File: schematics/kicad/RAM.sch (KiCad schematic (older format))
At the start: 4 parts

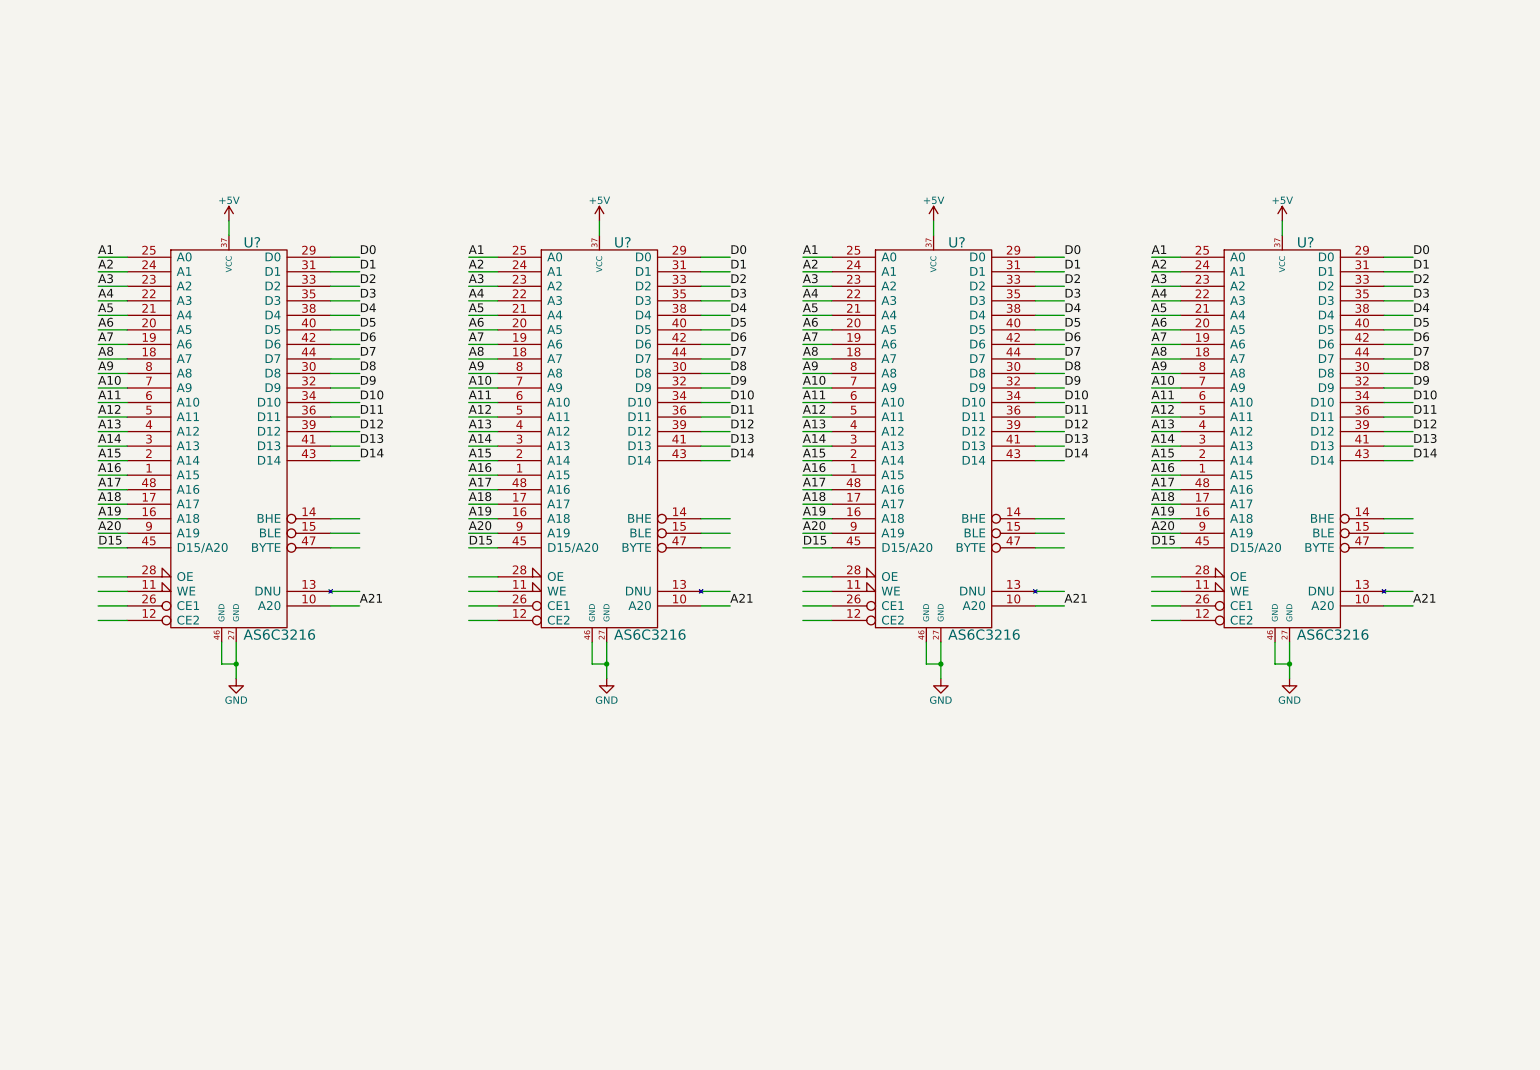
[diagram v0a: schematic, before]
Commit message: Add many hierarchical pins
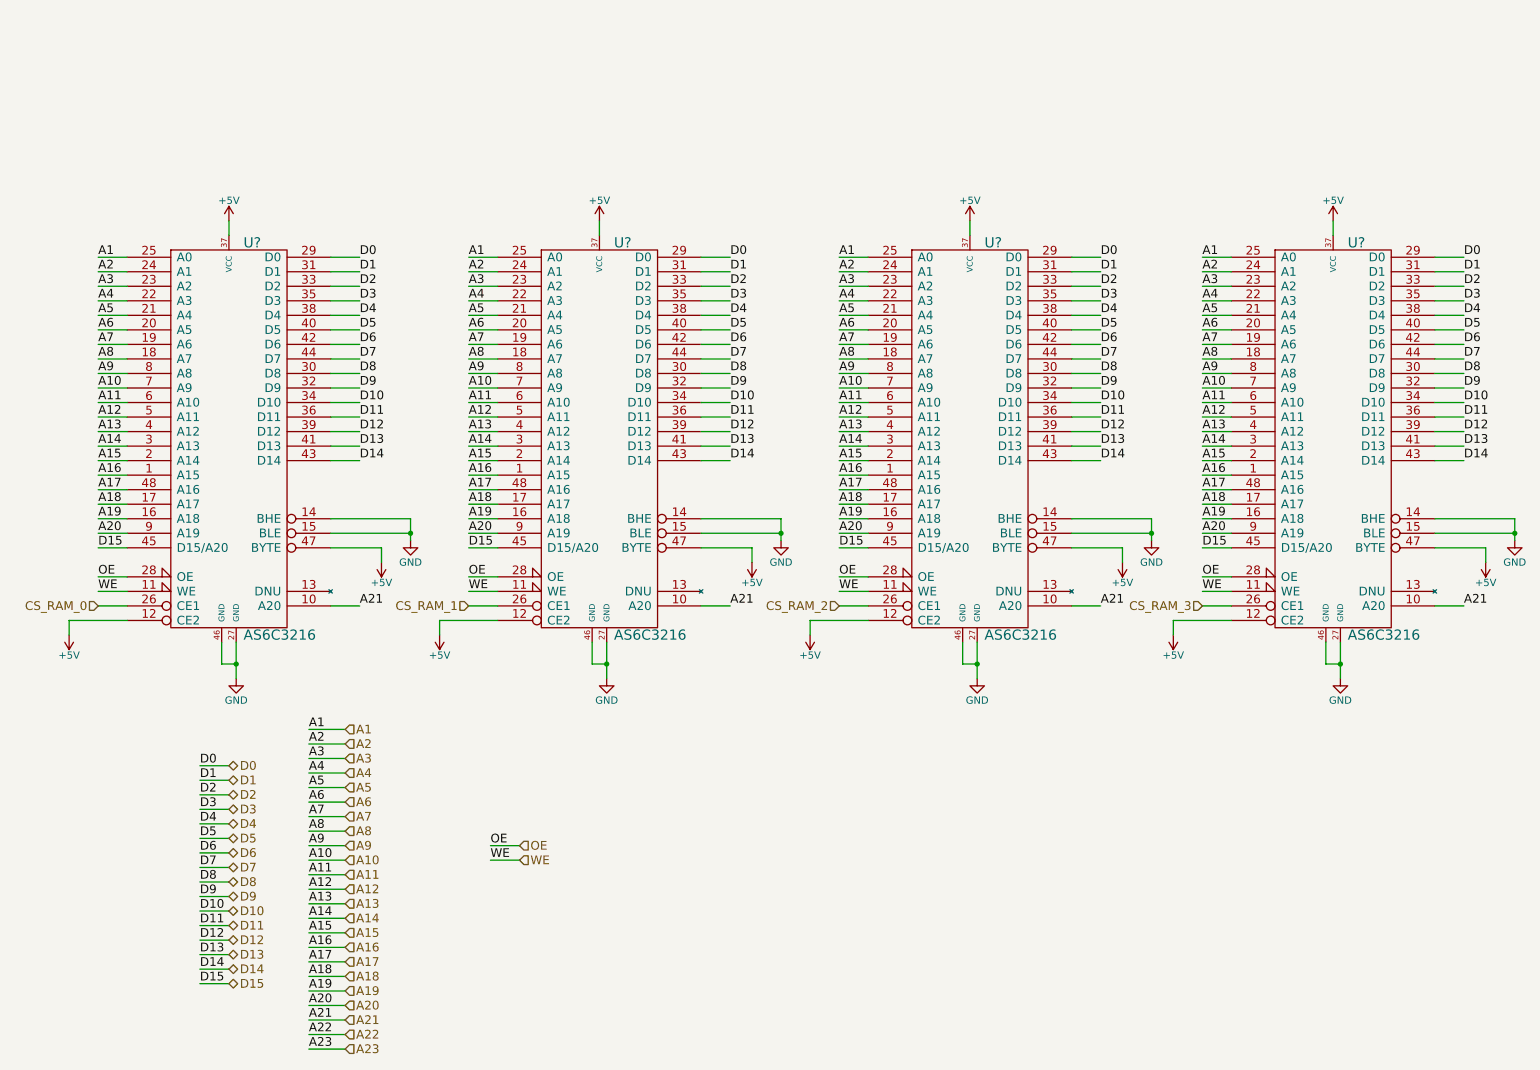
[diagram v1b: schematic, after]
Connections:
- net labels added: A22, A23, CS_RAM_0, CS_RAM_1, CS_RAM_2, CS_RAM_3, OE, WE
- wire segments 196 -> 245
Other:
- moved on the sheet: U?

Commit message: Change a lot of things, especially pinning between sheets
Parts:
- added C13, C14, C15, C16, C17, C18, C19, C20, C21, C22, C23, C24, C25, C26, C27, C28: 1u, symbol C
- gave numbers to parts that had none: 4
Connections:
- net +5V: now also C13.1, C14.1, C15.1, C16.1, C17.1, C18.1, C19.1, C20.1, C21.1, C22.1, C23.1, C24.1, C25.1, C26.1, C27.1, C28.1
- net GND: now also C13.2, C14.2, C15.2, C16.2, C17.2, C18.2, C19.2, C20.2, C21.2, C22.2, C23.2, C24.2, C25.2, C26.2, C27.2, C28.2
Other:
- note added: "Place next to RAM\n"
